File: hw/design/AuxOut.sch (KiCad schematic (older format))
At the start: 0 parts

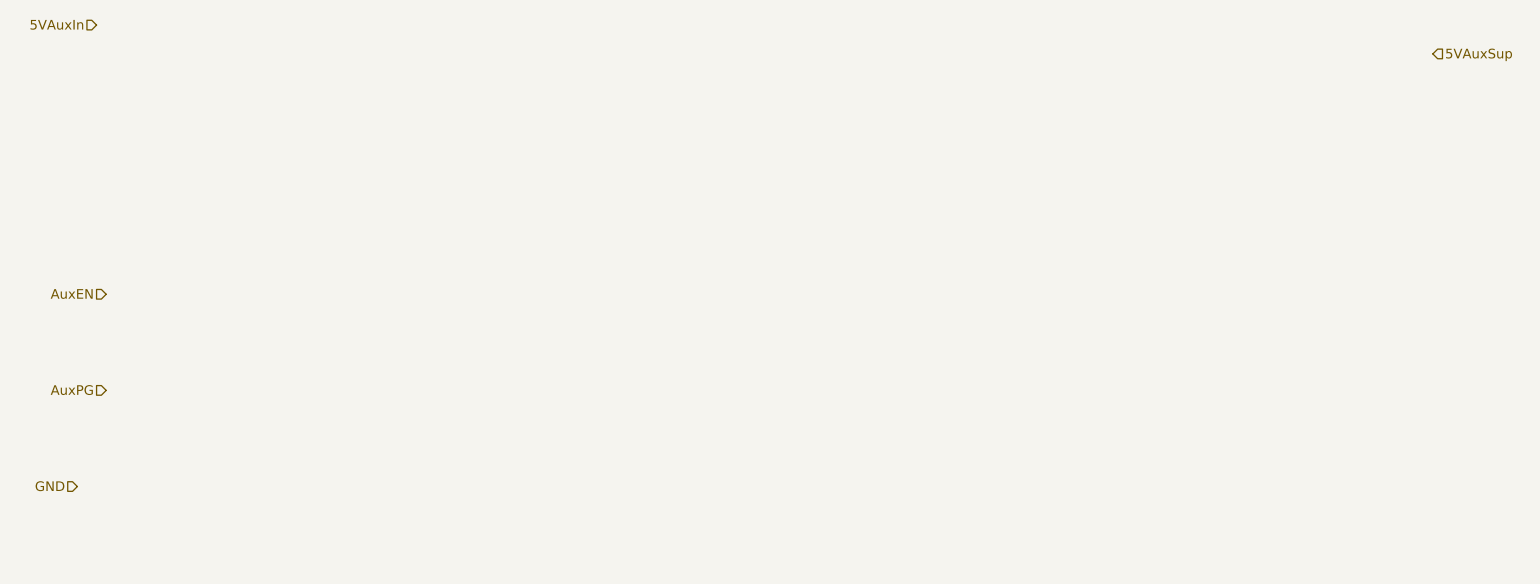
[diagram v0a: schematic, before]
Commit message: more work
more PFC work, more LDO work, added secondary regulator sheet, expanded system power tree sim
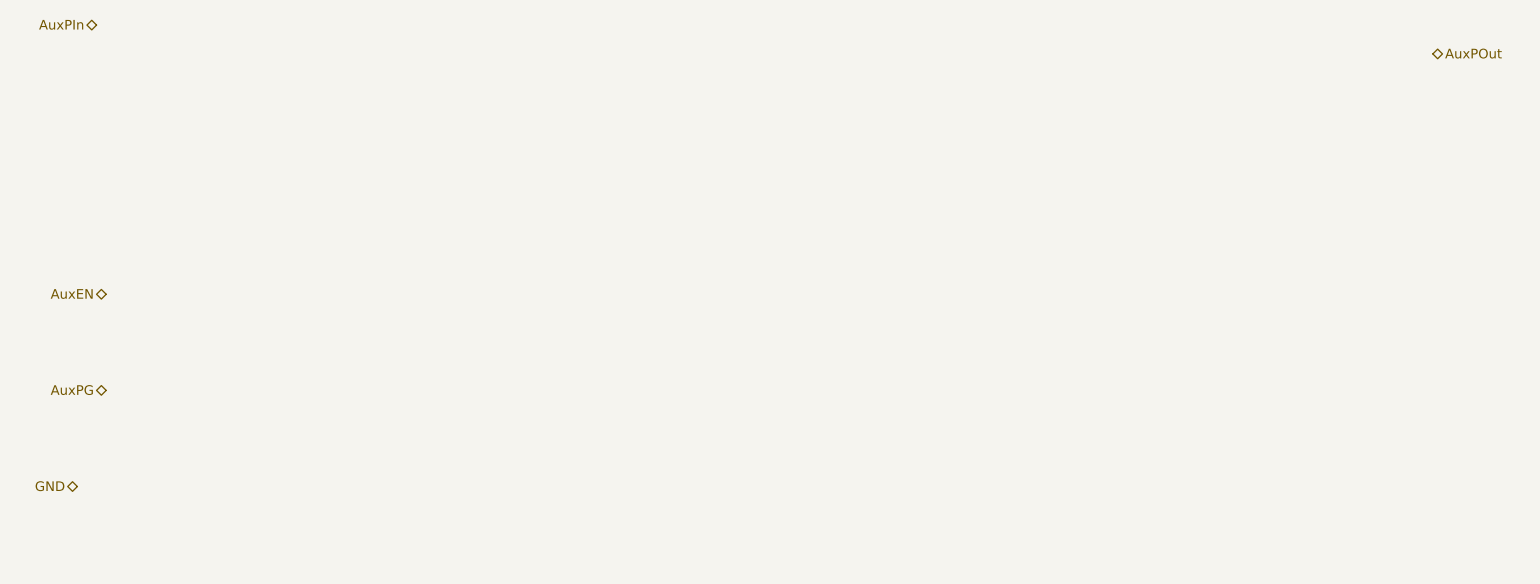
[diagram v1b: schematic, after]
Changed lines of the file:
@@
 $Descr A4 11693 8268
 encoding utf-8
-Sheet 7 7
+Sheet 7 8
 Title ""
 Date ""
@@
 Comment4 ""
 $EndDescr
-Text HLabel 1800 5350 0    50   Input ~ 0
+Text HLabel 1800 5350 0    50   BiDi ~ 0
 GND
-Text HLabel 8850 3100 2    50   Input ~ 0
-5VAuxSup
-Text HLabel 1900 2950 0    50   Input ~ 0
-5VAuxIn
-Text HLabel 1950 4350 0    50   Input ~ 0
+Text HLabel 8850 3100 2    50   BiDi ~ 0
+AuxPOut
+Text HLabel 1900 2950 0    50   BiDi ~ 0
+AuxPIn
+Text HLabel 1950 4350 0    50   BiDi ~ 0
 AuxEN
-Text HLabel 1950 4850 0    50   Input ~ 0
+Text HLabel 1950 4850 0    50   BiDi ~ 0
 AuxPG
 $EndSCHEMATC

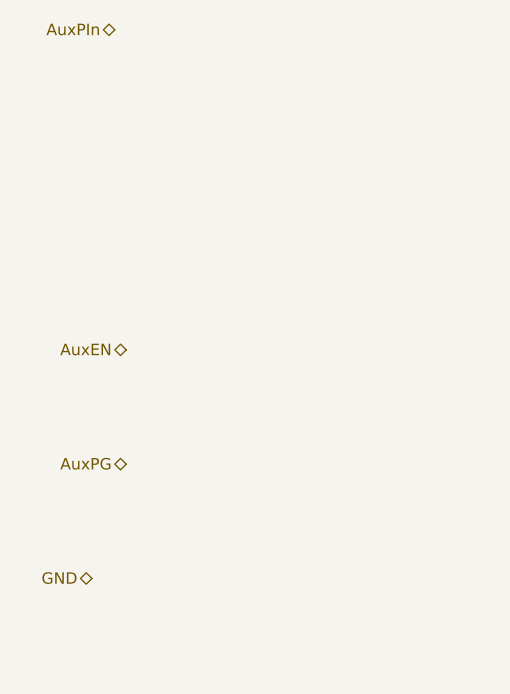
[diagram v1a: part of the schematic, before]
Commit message: lots of work
expanded README doc, specifications, added secondary regulator circuit + symbol, more component specs added
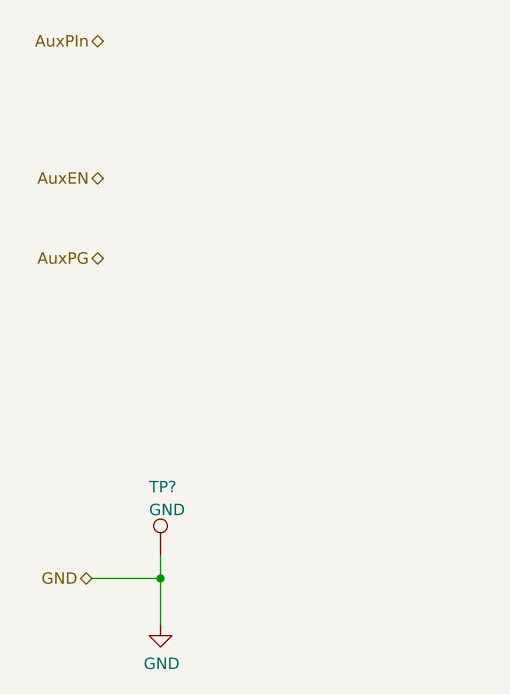
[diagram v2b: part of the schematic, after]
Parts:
- added TP?: GND, TestPoint:TestPoint_Keystone_5000-5004_Miniature, symbol Connector:TestPoint
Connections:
- net GND: now also TP?.1
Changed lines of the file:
@@
 $Descr A4 11693 8268
 encoding utf-8
-Sheet 7 8
+Sheet 8 8
 Title ""
 Date ""
@@
 Text HLabel 8850 3100 2    50   BiDi ~ 0
 AuxPOut
-Text HLabel 1900 2950 0    50   BiDi ~ 0
+Text HLabel 1850 3000 0    50   BiDi ~ 0
 AuxPIn
-Text HLabel 1950 4350 0    50   BiDi ~ 0
+Text HLabel 1850 3600 0    50   BiDi ~ 0
 AuxEN
-Text HLabel 1950 4850 0    50   BiDi ~ 0
+Text HLabel 1850 3950 0    50   BiDi ~ 0
 AuxPG
+$Comp
+L power:GND #PWR?
+U 1 1 5ECE7065
+P 2100 5550
+AR Path="/5ECE7065" Ref="#PWR?"  Part="1"
+AR Path="/5ECFB146/5ECE7065" Ref="#PWR?"  Part="1"
+F 0 "#PWR?" H 2100 5300 50  0001 C CNN
+F 1 "GND" H 2105 5377 50  0000 C CNN
+F 2 "" H 2100 5550 50  0001 C CNN
+F 3 "" H 2100 5550 50  0001 C CNN
+	1    2100 5550
+	1    0    0    -1
+$EndComp
+Wire Wire Line
+	2100 5350 2100 5550
+$Comp
+L Connector:TestPoint TP?
+U 1 1 5ECE706C
+P 2100 5250
+AR Path="/5E80D1C0/5ECE706C" Ref="TP?"  Part="1"
+AR Path="/5E80D210/5ECE706C" Ref="TP?"  Part="1"
+AR Path="/5E84FADE/5ECE706C" Ref="TP?"  Part="1"
+AR Path="/5ECFB146/5ECE706C" Ref="TP?"  Part="1"
+F 0 "TP?" H 2050 5550 50  0000 L CNN
+F 1 "GND" H 2050 5450 50  0000 L CNN
+F 2 "TestPoint:TestPoint_Keystone_5000-5004_Miniature" H 2300 5250 50  0001 C CNN
+F 3 "~" H 2300 5250 50  0001 C CNN
+	1    2100 5250
+	1    0    0    -1
+$EndComp
+Wire Wire Line
+	2100 5250 2100 5350
+Connection ~ 2100 5350
+Wire Wire Line
+	1800 5350 2100 5350
 $EndSCHEMATC
